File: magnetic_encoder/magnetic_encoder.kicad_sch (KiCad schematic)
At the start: 14 parts, among them IC1 AS5311-ATST, J1 Conn_01x07, J11 Conn_01x01, J12 Conn_01x01, J13 Conn_01x01, J17 Conn_01x01, J2 Conn_01x07

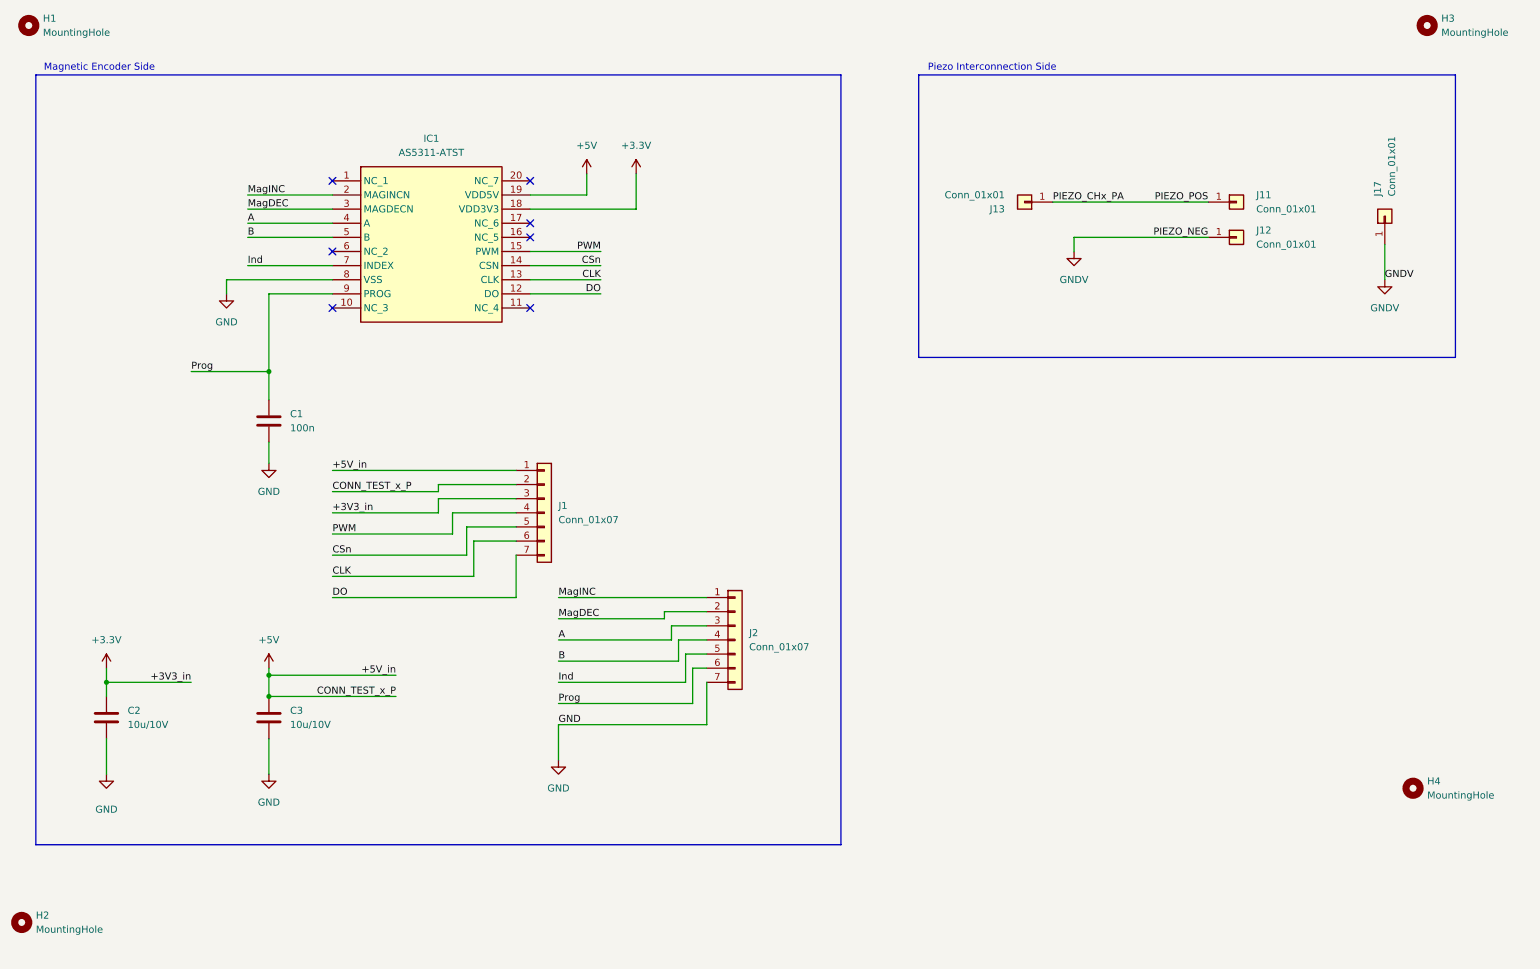
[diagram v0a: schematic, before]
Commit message: updated unused pins into testpoints
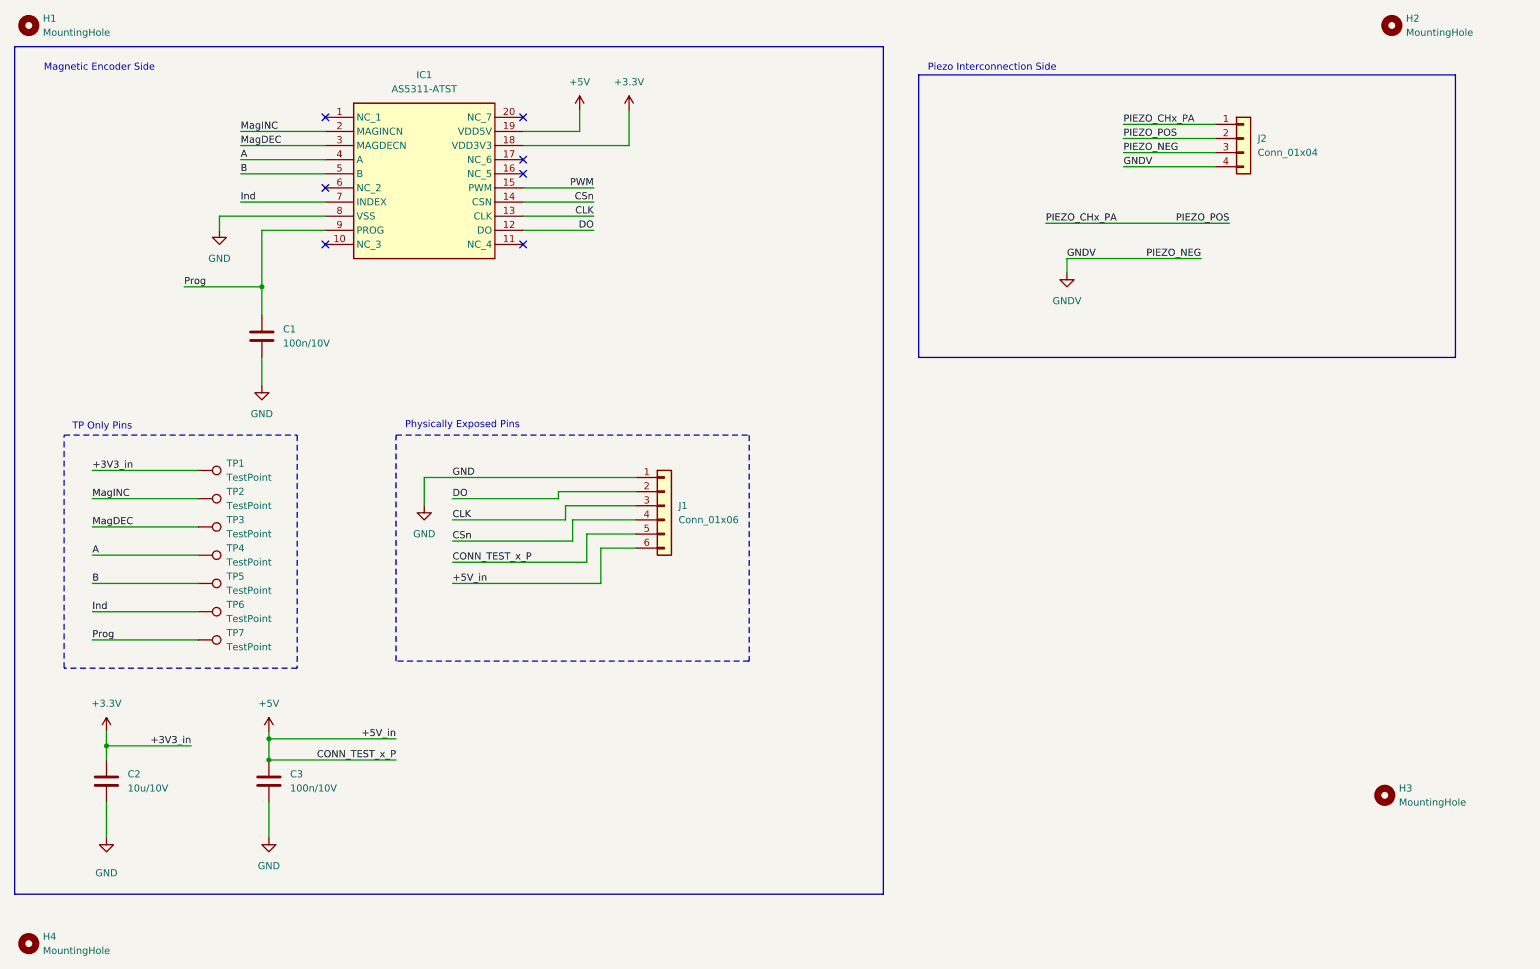
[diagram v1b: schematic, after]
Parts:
- removed H2: MountingHole, MountingHole:MountingHole_3.2mm_M3, symbol Mechanical:MountingHole
- removed J11, J12, J13, J17: Conn_01x01, TestPoint:TestPoint_THTPad_D2.5mm_Drill1.2mm, symbol Connector_Generic:Conn_01x01
- removed J2: Conn_01x07, Connector_PinSocket_2.54mm:PinSocket_1x07_P2.54mm_Vertical, symbol Connector_Generic:Conn_01x07
- added H4: MountingHole, MountingHole:MountingHole_3.2mm_M3, symbol Mechanical:MountingHole
- added J2: Conn_01x04, Connector_Wire:SolderWire-0.5sqmm_1x04_P4.6mm_D0.9mm_OD2.1mm_Relief, symbol Connector_Generic:Conn_01x04
- added TP1, TP2, TP3, TP4, TP5, TP6, TP7: TestPoint, TestPoint:TestPoint_Pad_D1.0mm, symbol Connector:TestPoint
- C1: value 100n -> 100n/10V
- C3: value 10u/10V -> 100n/10V
- J1: value Conn_01x07 -> Conn_01x06; footprint Connector_PinSocket_2.54mm:PinSocket_1x07_P2.54mm_Vertical -> Connector_Wire:SolderWire-0.5sqmm_1x06_P4.6mm_D0.9mm_OD2.1mm_Relief; symbol Connector_Generic:Conn_01x07 -> Connector_Generic:Conn_01x06
- renumbered H3 to H2, H4 to H3
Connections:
- net +3.3V: now also TP1.1; no longer J1.3 (Pin_3)
- net +5V: now also J1.5 (Pin_5), J1.6 (Pin_6); no longer J1.1 (Pin_1), J1.2 (Pin_2)
- net A: now also TP4.1
- net B: now also TP5.1
- net CLK: now also J1.3 (Pin_3); no longer J1.6 (Pin_6)
- net CSn: now also J1.4 (Pin_4); no longer J1.5 (Pin_5)
- net DO: now also J1.2 (Pin_2); no longer J1.7 (Pin_7)
- net GND: now also J1.1 (Pin_1)
- net GNDV: now also J2.3 (Pin_3), J2.4 (Pin_4)
- net Ind: now also TP6.1
- net MagDEC: now also TP3.1
- net MagINC: now also TP2.1
- net PIEZO_CHx_PA: now also J2.1 (Pin_1), J2.2 (Pin_2)
- net PWM: no longer J1.4 (Pin_4)
- net Prog: now also TP7.1
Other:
- note added: "Physically Exposed Pins"
- note added: "TP Only Pins"
- moved on the sheet: C1, C2, C3, H2, H3, IC1
